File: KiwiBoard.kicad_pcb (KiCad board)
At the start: 2 copper layers, 77 x 79.5 mm, 22 parts, among them J1 12V Power, J2 Heater, J3 Fan, J4 Motor Connector, J5 OLED, J6 Encoder Connector, K1 G5LE-14 DC3, Q1 PN2222A, Q2 TIP120, U1 Pico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

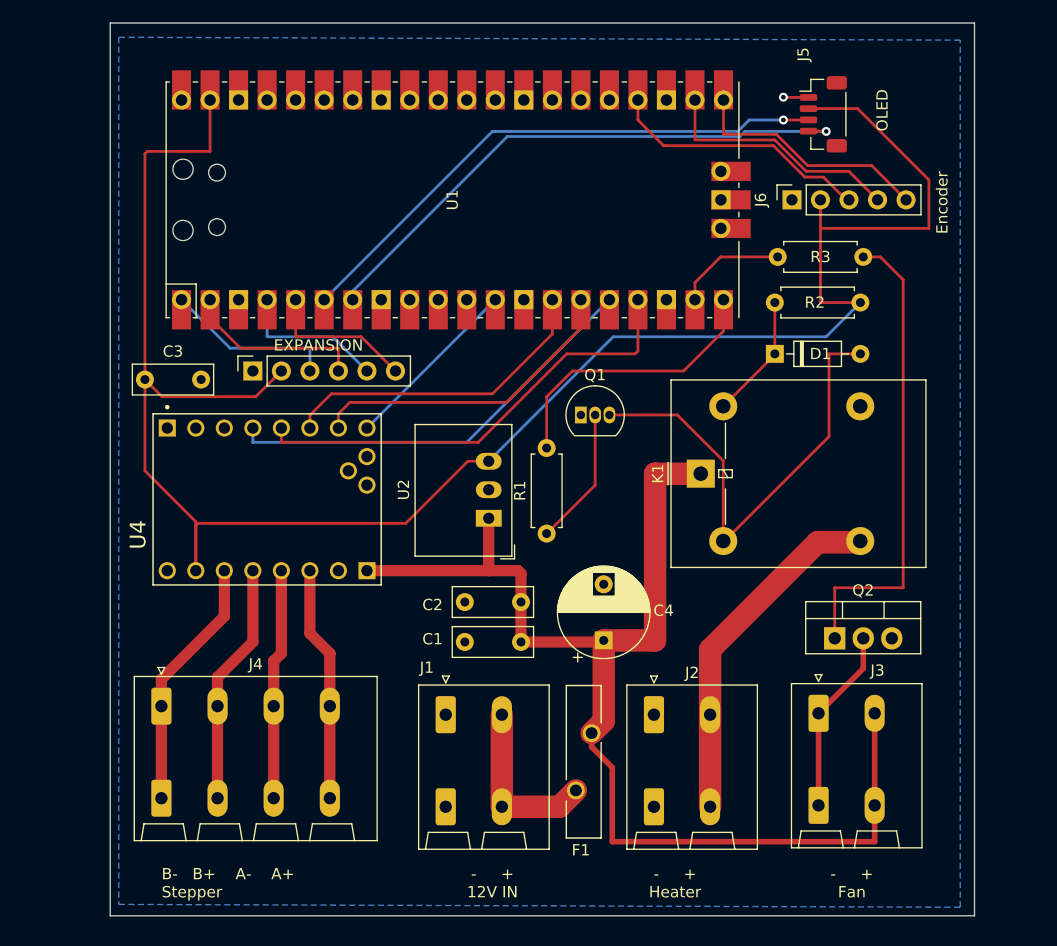
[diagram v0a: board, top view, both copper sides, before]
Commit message: Mechanical layout with original connectors
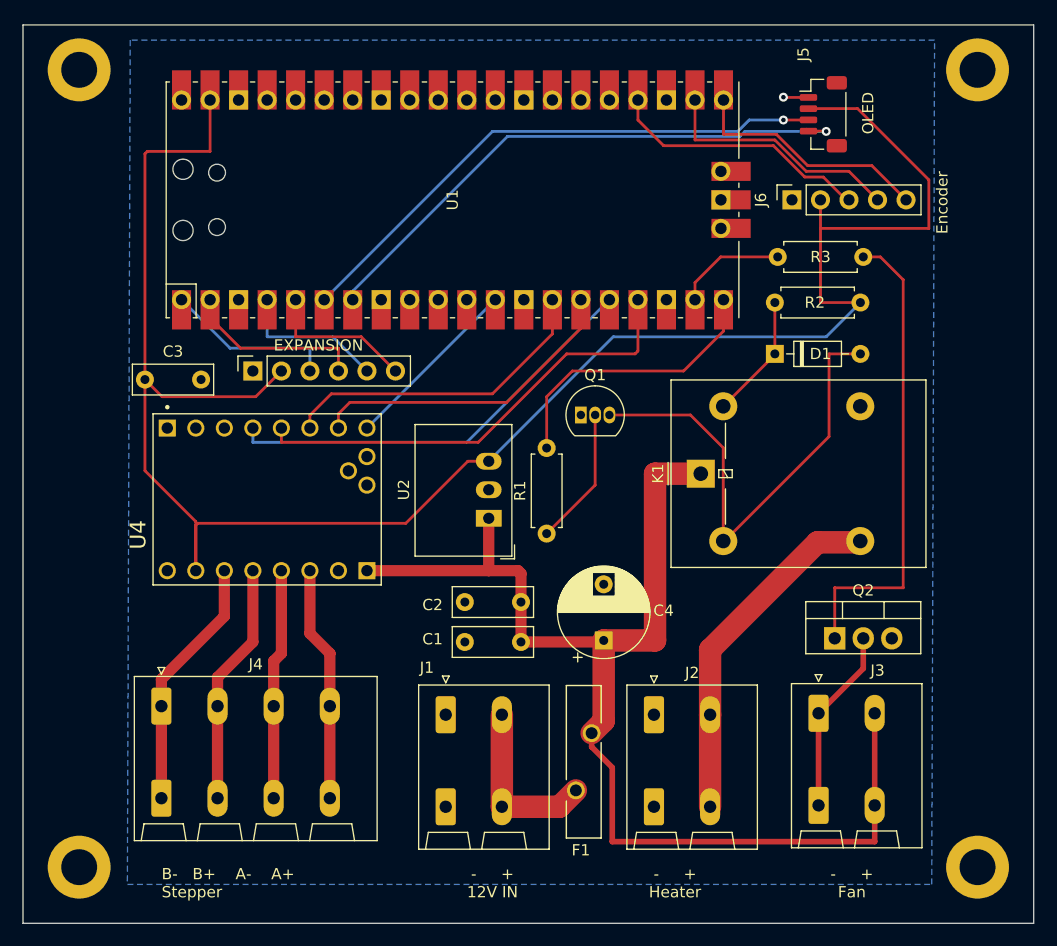
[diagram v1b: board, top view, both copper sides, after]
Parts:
- added ?: , , F.Cu at (126.0, 41.0)
- added ?: , , F.Cu at (46.0, 41.0)
- added ?: , , F.Cu at (126.0, 112.0)
- added REF**: MountingHole_3.2mm_M3_DIN965_Pad, MountingHole:MountingHole_3.2mm_M3_DIN965_Pad, F.Cu at (46.0, 112.0)
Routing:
- net Net-(D1-A): track 42.4 -> 43.1 mm
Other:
- board size 77 x 79.5 mm -> 90 x 80 mm
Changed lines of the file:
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@@
+      (rotate (xyz 0 0 0))
+    )
+    (model "C:/Users/2p3ca/Documents/Kicad/easyeda2kicad/easyeda2kicad.3dshapes/CONN-TH_P5.00_KF2EDGV-5.0-2P.wrl" hide
+      (offset (xyz 2.5 -8 0))
+      (scale (xyz 1 1 1))
       (rotate (xyz 0 0 0))
     )
@@
     )
   )
+  (footprint "" (layer "F.Cu")
+    (at 126 41)
+    (fp_text reference "" (at 0 0) (layer "F.SilkS")
+        (effects (font (size 1.27 1.27) (thickness 0.15)))
+    )
+    (fp_text value "" (at 0 0) (layer "F.SilkS")
+        (effects (font (size 1.27 1.27) (thickness 0.15)))
+    )
+    (pad "1" thru_hole circle (at 0 0) (size 5.6 5.6) (drill 3.2) (layers "*.Cu" "*.Mask"))
+  )
   (footprint "Package_TO_SOT_THT:TO-92_Inline" (layer "F.Cu")
     (at 90.678 71.734)
@@
       (rotate (xyz 0 0 0))
     )
+  )
+  (footprint "" (layer "F.Cu")
+    (at 46 41)
+    (fp_text reference "" (at 0 0) (layer "F.SilkS")
+        (effects (font (size 1.27 1.27) (thickness 0.15)))
+    )
+    (fp_text value "" (at 0 0) (layer "F.SilkS")
+        (effects (font (size 1.27 1.27) (thickness 0.15)))
+    )
+    (pad "1" thru_hole circle (at 0 0) (size 5.6 5.6) (drill 3.2) (layers "*.Cu" "*.Mask"))
   )
   (footprint "Connector_JST:JST_SH_BM04B-SRSS-TB_1x04-1MP_P1.00mm_Vertical" (layer "F.Cu")
@@
     (model "${KIPRJMOD}/project_library/3dmodel/pxc_1190297_02_LPT-2-5-2-5-0_3D.stp"
       (offset (xyz -3 -13.5 0))
+      (scale (xyz 1 1 1))
+      (rotate (xyz 0 0 0))
+    )
+    (model "C:/Users/2p3ca/Documents/Kicad/easyeda2kicad/easyeda2kicad.3dshapes/CONN-TH_P5.00_KF2EDGV-5.0-2P.wrl" hide
+      (offset (xyz 2.5 -8 0))
       (scale (xyz 1 1 1))
       (rotate (xyz 0 0 0))
@@
     )
   )
+  (footprint "MountingHole:MountingHole_3.2mm_M3_DIN965_Pad" (layer "F.Cu")
+    (at 46 112)
+    (descr "Mounting Hole 3.2mm, M3, DIN965")
+    (tags "mounting hole 3.2mm m3 din965")
+    (attr exclude_from_pos_files exclude_from_bom)
+    (fp_text reference "REF**" (at 0 -3.8) (layer "F.SilkS") hide
+        (effects (font (size 1 1) (thickness 0.15)))
+    )
+    (fp_text value "MountingHole_3.2mm_M3_DIN965_Pad" (at 0 3.8) (layer "F.Fab")
+        (effects (font (size 1 1) (thickness 0.15)))
+    )
+    (fp_text user "${REFERENCE}" (at 0 0) (layer "F.Fab")
+        (effects (font (size 1 1) (thickness 0.15)))
+    )
+    (fp_circle (center 0 0) (end 2.8 0)
+      (stroke (width 0.15) (type solid)) (fill none) (layer "Cmts.User"))
+    (fp_circle (center 0 0) (end 3.05 0)
+      (stroke (width 0.05) (type solid)) (fill none) (layer "F.CrtYd"))
+    (pad "1" thru_hole circle (at 0 0) (size 5.6 5.6) (drill 3.2) (layers "*.Cu" "*.Mask"))
+  )
   (footprint "Connector_Phoenix_SPT:PhoenixContact_SPT_2.5_2-H-5.0-EX_1x02_P5.0mm_Horizontal" (layer "F.Cu")
     (at 97.184 98.4225)
@@
     (model "${KIPRJMOD}/project_library/3dmodel/pxc_1190297_02_LPT-2-5-2-5-0_3D.stp"
       (offset (xyz -3 -13.5 0))
+      (scale (xyz 1 1 1))
+      (rotate (xyz 0 0 0))
+    )
+    (model "C:/Users/2p3ca/Documents/Kicad/easyeda2kicad/easyeda2kicad.3dshapes/CONN-TH_P5.00_KF2EDGV-5.0-2P.wrl" hide
+      (offset (xyz 2.5 -8.5 0))
       (scale (xyz 1 1 1))
       (rotate (xyz 0 0 0))
@@
       (rotate (xyz 0 0 0))
     )
+  )
+  (footprint "" (layer "F.Cu")
+    (at 126 112)
+    (fp_text reference "" (at 0 0) (layer "F.SilkS")
+        (effects (font (size 1.27 1.27) (thickness 0.15)))
+    )
+    (fp_text value "" (at 0 0) (layer "F.SilkS")
+        (effects (font (size 1.27 1.27) (thickness 0.15)))
+    )
+    (pad "1" thru_hole circle (at 0 0) (size 5.6 5.6) (drill 3.2) (layers "*.Cu" "*.Mask"))
   )
   (footprint "Connector_PinSocket_2.54mm:PinSocket_1x05_P2.54mm_Vertical" (layer "F.Cu")
@@
       (rotate (xyz 0 0 0))
     )
+    (model "C:/Users/2p3ca/Documents/Kicad/easyeda2kicad/easyeda2kicad.3dshapes/CONN-TH_4P-P5.00_KF2EDGV-5.0-4P.wrl" hide
+      (offset (xyz 7.5 -8 0))
+      (scale (xyz 1 1 1))
+      (rotate (xyz 0 0 0))
+    )
   )
   (footprint "Converter_DCDC:Converter_DCDC_RECOM_R-78E-0.5_THT" (layer "F.Cu")
@@
     (pad "5" thru_hole oval (at 6 2 90) (size 2.5 2.5) (drill 1.3) (layers "*.Cu" "*.Mask")
       (net 21 "Net-(D1-K)") (pintype "passive"))
-    (model "${KIPRJMOD}/project_library/3dmodel/G5LE-1A-EDC5.step"
+    (model "${KIPRJMOD}/project_library/3dmodel/G5LE-1A-EDC5.step" hide
       (offset (xyz 0 0 0))
       (scale (xyz 1 1 1))
       (rotate (xyz -90 0 90))
+    )
+    (model "${KIPRJMOD}/project_library/3dmodel/easyeda2kicad.3dshapes/RELAY-TH_L19.2-W15.6-H15.8.wrl"
+      (offset (xyz -6.5 0 5.5))
+      (scale (xyz 1 1 1))
+      (rotate (xyz 0 0 90))
     )
   )
@@
     )
   )
-  (gr_rect (start 48.768 36.83) (end 125.73 116.332)
+  (gr_rect (start 41 37) (end 131 117)
     (stroke (width 0.1) (type default)) (fill none) (layer "Edge.Cuts"))
   (gr_text "^^ INSERT ELECTRONS HERE ^^" (at 87.376 97.028 90) (layer "B.SilkS")
@@
     (effects (font (size 1 1) (thickness 0.15)) (justify left bottom))
   )
-  (gr_text "OLED" (at 118.11 46.482 90) (layer "F.SilkS")
+  (gr_text "OLED" (at 116.84 46.736 90) (layer "F.SilkS")
     (effects (font (size 1 1) (thickness 0.15)) (justify left bottom))
   )
@@
   (gr_text "-     +\n12V IN  " (at 82.804 114.808) (layer "F.SilkS")
     (effects (font (size 1 1) (thickness 0.15)) (justify bottom))
+  )
+  (dimension (type aligned) (layer "User.1")
+    (pts (xy 131 117) (xy 131 37))
+    (height 9)
+    (gr_text "80.0000 mm" (at 138.85 77 90) (layer "User.1")
+      (effects (font (size 1 1) (thickness 0.15)))
+    )
+    (format (prefix "") (suffix "") (units 3) (units_format 1) (precision 4))
+    (style (thickness 0.15) (arrow_length 1.27) (text_position_mode 0) (extension_height 0.58642) (extension_offset 0.5) keep_text_aligned)
+  )
+  (dimension (type aligned) (layer "User.1")
+    (pts (xy 131 117) (xy 41 117))
+    (height -3)
+    (gr_text "90.0000 mm" (at 86 118.85) (layer "User.1")
+      (effects (font (size 1 1) (thickness 0.15)))
+    )
+    (format (prefix "") (suffix "") (units 3) (units_format 1) (precision 4))
+    (style (thickness 0.15) (arrow_length 1.27) (text_position_mode 0) (extension_height 0.58642) (extension_offset 0.5) keep_text_aligned)
+  )
+  (dimension (type aligned) (layer "User.1")
+    (pts (xy 126 41) (xy 46 41))
+    (height 8)
+    (gr_text "80.0000 mm" (at 86 31.85) (layer "User.1")
+      (effects (font (size 1 1) (thickness 0.15)))
+    )
+    (format (prefix "") (suffix "") (units 3) (units_format 1) (precision 4))
+    (style (thickness 0.15) (arrow_length 1.27) (text_position_mode 0) (extension_height 0.58642) (extension_offset 0.5) keep_text_aligned)
+  )
+  (dimension (type aligned) (layer "User.1")
+    (pts (xy 126 112) (xy 126 41))
+    (height 9)
+    (gr_text "71.0000 mm" (at 133.85 76.5 90) (layer "User.1")
+      (effects (font (size 1 1) (thickness 0.15)))
+    )
+    (format (prefix "") (suffix "") (units 3) (units_format 1) (precision 4))
+    (style (thickness 0.15) (arrow_length 1.27) (text_position_mode 0) (extension_height 0.58642) (extension_offset 0.5) keep_text_aligned)
   )
   (segment (start 82.4715 85.598) (end 85.09 85.598) (width 1) (layer "F.Cu") (net 19))
@@
   (segment (start 107.95 66.3665) (end 103.3545 70.962) (width 0.25) (layer "F.Cu") (net 21))
   (segment (start 103.3545 82.962) (end 103.474 82.962) (width 0.25) (layer "F.Cu") (net 22))
-  (segment (start 93.218 71.734) (end 99.2765 71.734) (width 0.25) (layer "F.Cu") (net 22))
-  (segment (start 99.2765 71.734) (end 103.3545 75.812) (width 0.25) (layer "F.Cu") (net 22))
+  (segment (start 103.3545 74.6525) (end 103.3545 82.962) (width 0.25) (layer "F.Cu") (net 22))
   (segment (start 112.776 66.294) (end 115.57 66.294) (width 0.25) (layer "F.Cu") (net 22))
-  (segment (start 103.3545 75.812) (end 103.3545 82.962) (width 0.25) (layer "F.Cu") (net 22))
+  (segment (start 100.436 71.734) (end 103.3545 74.6525) (width 0.25) (layer "F.Cu") (net 22))
   (segment (start 103.474 82.962) (end 112.776 73.66) (width 0.25) (layer "F.Cu") (net 22))
+  (segment (start 93.218 71.734) (end 100.436 71.734) (width 0.25) (layer "F.Cu") (net 22))
   (segment (start 112.776 73.66) (end 112.776 66.294) (width 0.25) (layer "F.Cu") (net 22))
   (segment (start 115.5545 83.0735) (end 115.5545 82.962) (width 0.8) (layer "F.Cu") (net 23))
@@
     (polygon
       (pts
-        (xy 49.53 38.1)
-        (xy 49.53 115.316)
-        (xy 124.46 115.57)
-        (xy 124.46 38.354)
+        (xy 50.546 38.354)
+        (xy 50.292 113.538)
+        (xy 121.92 113.538)
+        (xy 122.174 38.354)
       )
     )

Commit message: Change to JST PH connectors for OLED and Encoder.  Adjust spacing for the 3v3 regulator
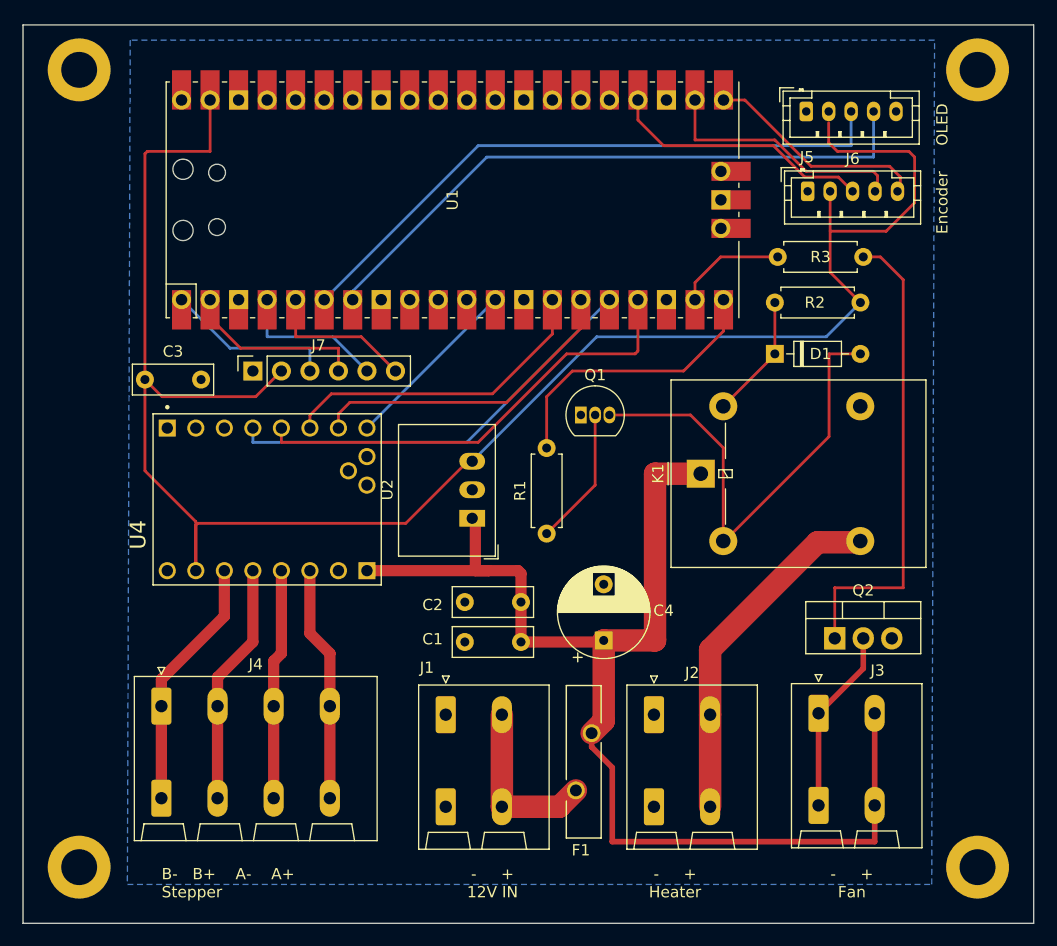
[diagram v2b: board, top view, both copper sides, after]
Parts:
- removed ? (x3): , 
- added REF**: MountingHole_3.2mm_M3_DIN965_Pad, MountingHole:MountingHole_3.2mm_M3_DIN965_Pad, F.Cu at (46.0, 41.0)
- added REF**: MountingHole_3.2mm_M3_DIN965_Pad, MountingHole:MountingHole_3.2mm_M3_DIN965_Pad, F.Cu at (126.0, 41.0)
- added REF**: MountingHole_3.2mm_M3_DIN965_Pad, MountingHole:MountingHole_3.2mm_M3_DIN965_Pad, F.Cu at (126.0, 112.0)
- J5: footprint Connector_JST:JST_SH_BM04B-SRSS-TB_1x04-1MP_P1.00mm_Vertical -> Connector_JST:JST_PH_B5B-PH-K_1x05_P2.00mm_Vertical
- J6: footprint Connector_PinSocket_2.54mm:PinSocket_1x05_P2.54mm_Vertical -> Connector_JST:JST_PH_B5B-PH-K_1x05_P2.00mm_Vertical
- moved J6 1.59 mm to (110.9, 51.8), turned to 0 degrees
- moved J5 1.55 mm to (110.7, 44.7), turned to 0 degrees
- moved U2 1.47 mm to (81.0, 80.9)
- renumbered EXPANSION to J7
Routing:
- net +3.3V: track 174.7 -> 167.9 mm
- net SDA: track 49.8 -> 55.7 mm, vias 1 -> 0
- net SLC: track 50.6 -> 56.2 mm, vias 1 -> 0
- net GND: track 2.24 -> 0.00 mm, vias 1 -> 0
- net ENC2: track 21.7 -> 20.1 mm
- net +12V: track 109.4 -> 110.7 mm
- net ENC1: track 22.0 -> 23.3 mm

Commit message: Change to 2p connectors for the motor.  Retaining the ability to use the 2row connectors or one row connectors
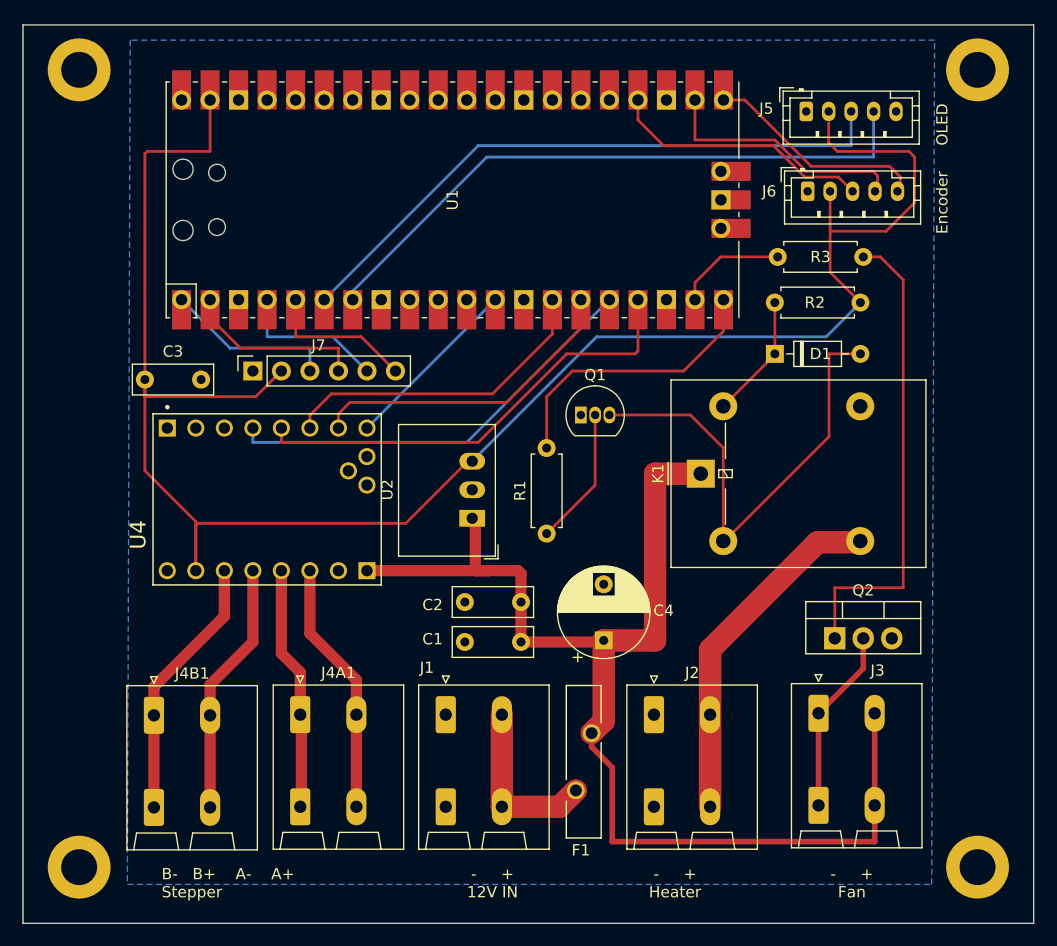
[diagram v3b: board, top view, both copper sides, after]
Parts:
- removed J4: Motor Connector, Library:PhoenixContact_LPT_2.5_4-H-5.0_1x04_P5.0mm_Horizontal
- added J4A1: Motor A, Connector_Phoenix_SPT:PhoenixContact_SPT_2.5_2-H-5.0-EX_1x02_P5.0mm_Horizontal, F.Cu at (65.7, 98.4)
- added J4B1: Motor B, Connector_Phoenix_SPT:PhoenixContact_SPT_2.5_2-H-5.0-EX_1x02_P5.0mm_Horizontal, F.Cu at (52.7, 98.5)
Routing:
- net A-: track 20.5 -> 21.8 mm
- net B-: track 22.6 -> 23.7 mm
- net B+: track 21.6 -> 22.7 mm
- net A+: track 21.0 -> 22.0 mm
- net +3.3V: track 167.9 -> 168.8 mm

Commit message: reworked with JST PH connectors, move raspi to board edge
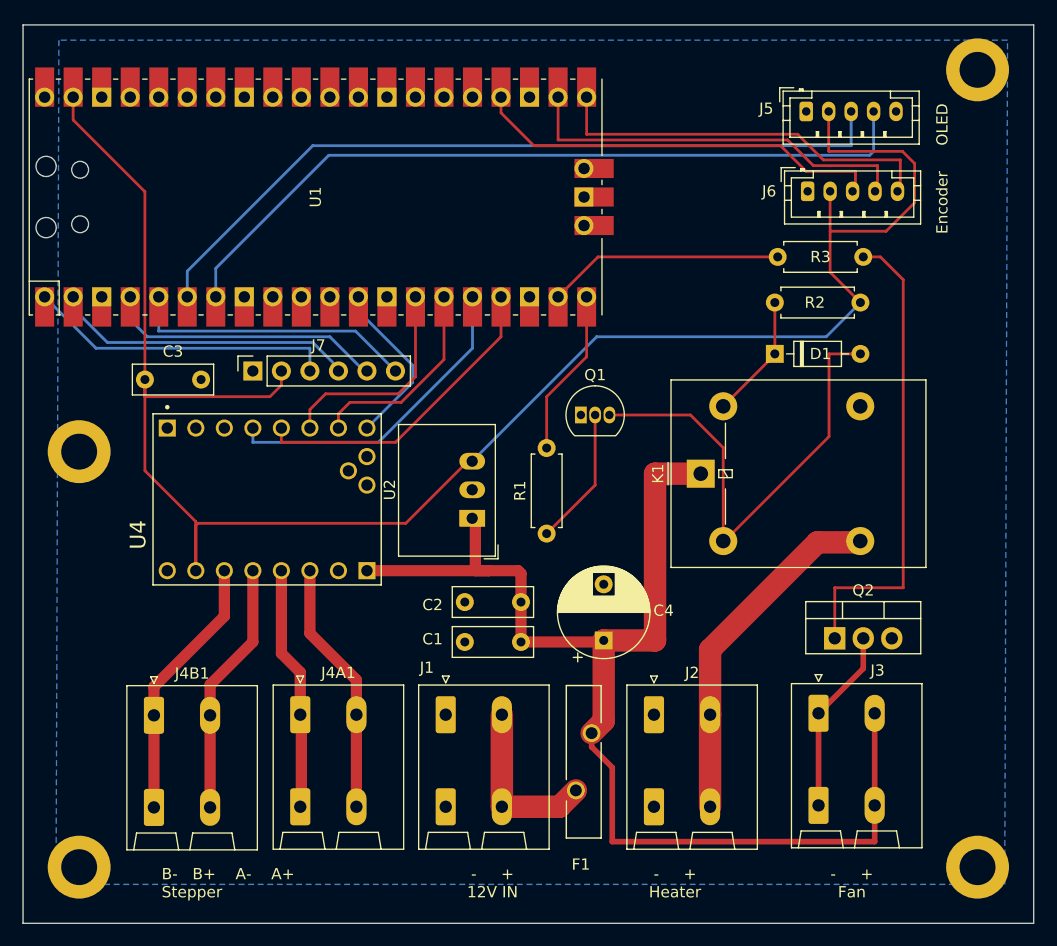
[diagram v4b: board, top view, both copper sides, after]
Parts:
- moved REF** 34.0 mm to (46.0, 75.0)
- moved U1 12.2 mm to (67.1, 52.3)
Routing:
- net ENC2: track 20.1 -> 35.2 mm
- net SDA: track 55.7 -> 69.1 mm
- net ENC1: track 23.3 -> 36.3 mm
- net SLC: track 56.2 -> 69.0 mm
- net SS: track 41.0 -> 28.3 mm
- net EXT1: track 15.3 -> 27.5 mm
- net EXT4: track 13.5 -> 25.6 mm
- net EXT3: track 13.5 -> 25.0 mm
- net FAN_CTL: track 9.84 -> 21.0 mm
- net BTN: track 26.2 -> 37.1 mm
- net EXT2: track 16.2 -> 27.1 mm
- net HEATER_CTL: track 25.5 -> 14.9 mm
- net MOSI: track 28.6 -> 18.3 mm
- net SCLK: track 28.8 -> 19.4 mm
- net MISO: track 38.3 -> 28.9 mm
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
